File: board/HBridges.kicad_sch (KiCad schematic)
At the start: 36 parts, among them Q1 NMOS, Q2 NMOS, Q3 NMOS, Q4 NMOS, Q5 NMOS, Q6 NMOS

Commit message: Added CAN and Encoder connectors.
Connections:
- net VCC renamed VM
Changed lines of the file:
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@@
 			)
 		)
-		(property "Value" "VCC"
-			(at 41.91 22.86 0)
-			(effects
-				(font
-					(size 1.27 1.27)
-				)
+		(property "Value" "VM"
+			(at 44.45 26.6699 0)
+			(effects
+				(font
+					(size 1.27 1.27)
+				)
+				(justify left)
 			)
 		)
@@
 			)
 		)
-		(property "Value" "VCC"
-			(at 88.9 22.86 0)
-			(effects
-				(font
-					(size 1.27 1.27)
-				)
+		(property "Value" "VM"
+			(at 91.44 26.6699 0)
+			(effects
+				(font
+					(size 1.27 1.27)
+				)
+				(justify left)
 			)
 		)
@@
 			)
 		)
-		(property "Value" "VCC"
-			(at 135.89 22.86 0)
-			(effects
-				(font
-					(size 1.27 1.27)
-				)
-			)
-		)
+		(property "Value" "VM"
+			(at 138.43 26.6699 0)
+			(effects
+				(font
+					(size 1.27 1.27)
+				)
+				(justify left)
+			)
+		)

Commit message: Added some resistor and capacitor values.
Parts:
- C1, C10, C8: value C -> 30 nF
- R1, R11, R12, R2, R8, R9: value R -> 18 Ω
- R10, R13, R3: value R -> 1 mΩ / 1%
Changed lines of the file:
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@@
 			)
 		)
-		(property "Value" "R"
+		(property "Value" "18 Ω"
 			(at 121.92 39.37 90)
 			(effects
@@
 			)
 		)
-		(property "Value" "R"
+		(property "Value" "18 Ω"
 			(at 122.174 59.69 90)
 			(effects
@@
 			)
 		)
-		(property "Value" "R"
+		(property "Value" "18 Ω"
 			(at 28.194 59.69 90)
 			(effects
@@
 			)
 		)
-		(property "Value" "R"
+		(property "Value" "18 Ω"
 			(at 27.94 39.37 90)
 			(effects
@@
 			)
 		)
-		(property "Value" "R"
+		(property "Value" "18 Ω"
 			(at 75.184 59.69 90)
 			(effects
@@
 			)
 		)
-		(property "Value" "C"
+		(property "Value" "30 nF"
 			(at 129.794 50.8 90)
 			(effects
@@
 			)
 		)
-		(property "Value" "R"
-			(at 135.89 73.914 90)
+		(property "Value" "1 mΩ / 1%"
+			(at 133.604 73.66 90)
 			(effects
 				(font
@@
 			)
 		)
-		(property "Value" "R"
-			(at 41.91 73.914 90)
+		(property "Value" "1 mΩ / 1%"
+			(at 39.37 73.66 90)
 			(effects
 				(font
@@
 			)
 		)
-		(property "Value" "C"
+		(property "Value" "30 nF"
 			(at 82.804 50.8 90)
 			(effects
@@
 			)
 		)
-		(property "Value" "C"
+		(property "Value" "30 nF"
 			(at 35.814 50.8 90)
 			(effects
@@
 			)
 		)
-		(property "Value" "R"
-			(at 88.9 73.914 90)
+		(property "Value" "1 mΩ / 1%"
+			(at 86.868 73.914 90)
 			(effects
 				(font
@@
 			)
 		)
-		(property "Value" "R"
+		(property "Value" "18 Ω"
 			(at 74.93 39.37 90)
 			(effects

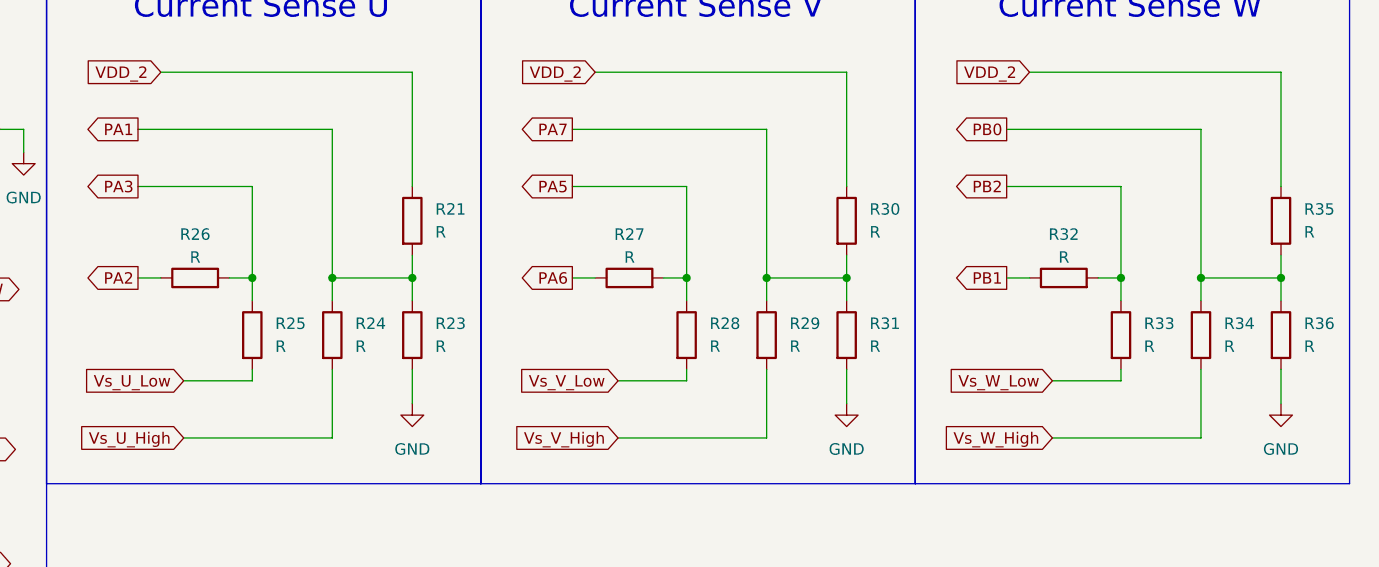
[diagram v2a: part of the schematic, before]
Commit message: Added resistor values to current sense circuit.
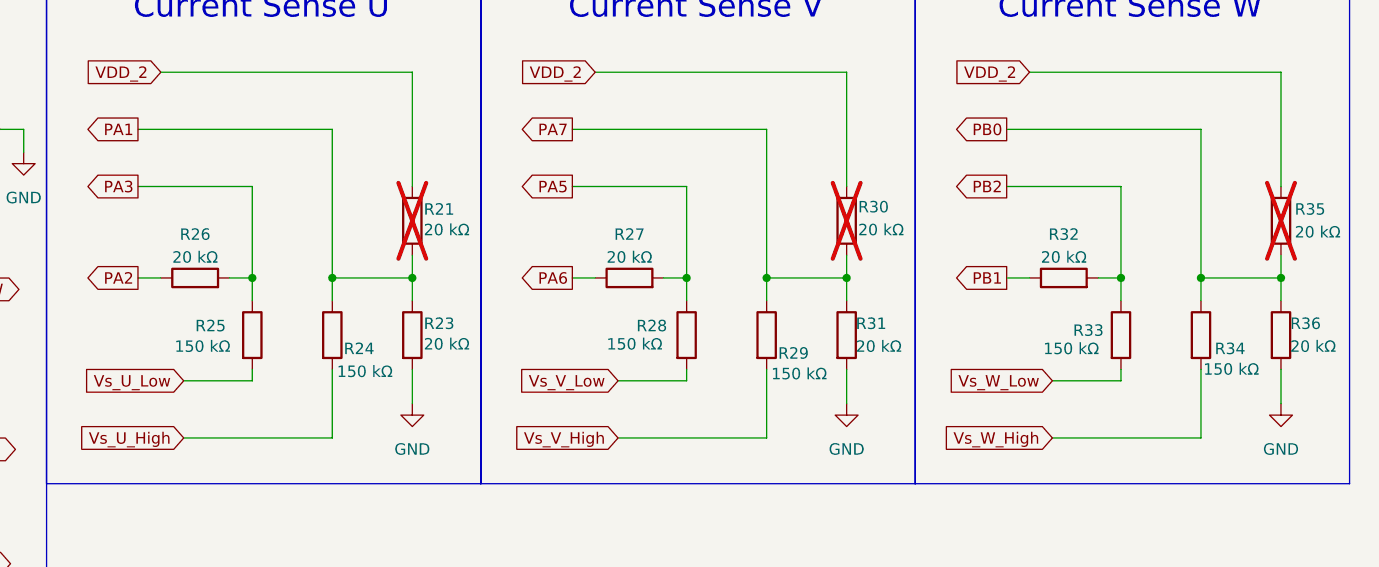
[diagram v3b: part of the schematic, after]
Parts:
- R21, R30, R35: value R -> 20 kΩ; now not fitted
- R23, R26, R27, R31, R32, R36: value R -> 20 kΩ
- R24, R25, R28, R29, R33, R34: value R -> 150 kΩ
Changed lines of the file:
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@@
 		(in_bom yes)
 		(on_board yes)
-		(dnp no)
-		(fields_autoplaced yes)
+		(dnp yes)
 		(property "Reference" "R30"
-			(at 245.11 40.6399 0)
-			(effects
-				(font
-					(size 1.27 1.27)
-				)
-				(justify left)
-			)
-		)
-		(property "Value" "R"
-			(at 245.11 43.1799 0)
+			(at 243.84 40.386 0)
+			(effects
+				(font
+					(size 1.27 1.27)
+				)
+				(justify left)
+			)
+		)
+		(property "Value" "20 kΩ"
+			(at 243.84 42.926 0)
 			(effects
 				(font
@@
 		(on_board yes)
 		(dnp no)
-		(fields_autoplaced yes)
 		(property "Reference" "R25"
-			(at 179.07 53.3399 0)
-			(effects
-				(font
-					(size 1.27 1.27)
-				)
-				(justify left)
-			)
-		)
-		(property "Value" "R"
-			(at 179.07 55.8799 0)
+			(at 170.18 53.594 0)
+			(effects
+				(font
+					(size 1.27 1.27)
+				)
+				(justify left)
+			)
+		)
+		(property "Value" "150 kΩ"
+			(at 167.894 55.88 0)
 			(effects
 				(font
@@
 			)
 		)
-		(property "Value" "R"
+		(property "Value" "20 kΩ"
 			(at 218.44 45.974 90)
 			(effects
@@
 		(in_bom yes)
 		(on_board yes)
-		(dnp no)
-		(fields_autoplaced yes)
+		(dnp yes)
 		(property "Reference" "R35"
-			(at 293.37 40.6399 0)
-			(effects
-				(font
-					(size 1.27 1.27)
-				)
-				(justify left)
-			)
-		)
-		(property "Value" "R"
-			(at 293.37 43.1799 0)
+			(at 292.354 40.64 0)
+			(effects
+				(font
+					(size 1.27 1.27)
+				)
+				(justify left)
+			)
+		)
+		(property "Value" "20 kΩ"
+			(at 292.354 43.18 0)
 			(effects
 				(font
@@
 			)
 		)
-		(property "Value" "R"
+		(property "Value" "20 kΩ"
 			(at 266.7 45.974 90)
 			(effects
@@
 		(in_bom yes)
 		(on_board yes)
-		(dnp no)
-		(fields_autoplaced yes)
+		(dnp yes)
 		(property "Reference" "R21"
-			(at 196.85 40.6399 0)
-			(effects
-				(font
-					(size 1.27 1.27)
-				)
-				(justify left)
-			)
-		)
-		(property "Value" "R"
-			(at 196.85 43.1799 0)
+			(at 195.58 40.64 0)
+			(effects
+				(font
+					(size 1.27 1.27)
+				)
+				(justify left)
+			)
+		)
+		(property "Value" "20 kΩ"
+			(at 195.58 42.926 0)
 			(effects
 				(font
@@
 		(on_board yes)
 		(dnp no)
-		(fields_autoplaced yes)
 		(property "Reference" "R33"
-			(at 275.59 53.3399 0)
-			(effects
-				(font
-					(size 1.27 1.27)
-				)
-				(justify left)
-			)
-		)
-		(property "Value" "R"
-			(at 275.59 55.8799 0)
+			(at 267.716 54.102 0)
+			(effects
+				(font
+					(size 1.27 1.27)
+				)
+				(justify left)
+			)
+		)
+		(property "Value" "150 kΩ"
+			(at 264.414 56.134 0)
 			(effects
 				(font
@@
 		(on_board yes)
 		(dnp no)
-		(fields_autoplaced yes)
 		(property "Reference" "R24"
-			(at 187.96 53.3399 0)
-			(effects
-				(font
-					(size 1.27 1.27)
-				)
-				(justify left)
-			)
-		)
-		(property "Value" "R"
-			(at 187.96 55.8799 0)
+			(at 186.69 56.134 0)
+			(effects
+				(font
+					(size 1.27 1.27)
+				)
+				(justify left)
+			)
+		)
+		(property "Value" "150 kΩ"
+			(at 185.928 58.674 0)
 			(effects
 				(font
@@
 		(on_board yes)
 		(dnp no)
-		(fields_autoplaced yes)
 		(property "Reference" "R31"
-			(at 245.11 53.3399 0)
-			(effects
-				(font
-					(size 1.27 1.27)
-				)
-				(justify left)
-			)
-		)
-		(property "Value" "R"
-			(at 245.11 55.8799 0)
+			(at 243.586 53.34 0)
+			(effects
+				(font
+					(size 1.27 1.27)
+				)
+				(justify left)
+			)
+		)
+		(property "Value" "20 kΩ"
+			(at 243.586 55.88 0)
 			(effects
 				(font
@@
 		(on_board yes)
 		(dnp no)
-		(fields_autoplaced yes)
 		(property "Reference" "R34"
-			(at 284.48 53.3399 0)
-			(effects
-				(font
-					(size 1.27 1.27)
-				)
-				(justify left)
-			)
-		)
-		(property "Value" "R"
-			(at 284.48 55.8799 0)
+			(at 283.464 56.134 0)
+			(effects
+				(font
+					(size 1.27 1.27)
+				)
+				(justify left)
+			)
+		)
+		(property "Value" "150 kΩ"
+			(at 282.194 58.42 0)
 			(effects
 				(font
@@
 		(on_board yes)
 		(dnp no)
-		(fields_autoplaced yes)
 		(property "Reference" "R28"
-			(at 227.33 53.3399 0)
-			(effects
-				(font
-					(size 1.27 1.27)
-				)
-				(justify left)
-			)
-		)
-		(property "Value" "R"
-			(at 227.33 55.8799 0)
+			(at 219.202 53.594 0)
+			(effects
+				(font
+					(size 1.27 1.27)
+				)
+				(justify left)
+			)
+		)
+		(property "Value" "150 kΩ"
+			(at 215.9 55.626 0)
 			(effects
 				(font
@@
 		(on_board yes)
 		(dnp no)
-		(fields_autoplaced yes)
 		(property "Reference" "R23"
-			(at 196.85 53.3399 0)
-			(effects
-				(font
-					(size 1.27 1.27)
-				)
-				(justify left)
-			)
-		)
-		(property "Value" "R"
-			(at 196.85 55.8799 0)
+			(at 195.58 53.34 0)
+			(effects
+				(font
+					(size 1.27 1.27)
+				)
+				(justify left)
+			)
+		)
+		(property "Value" "20 kΩ"
+			(at 195.58 55.626 0)
 			(effects
 				(font
@@
 			)
 		)
-		(property "Value" "R"
+		(property "Value" "20 kΩ"
 			(at 170.18 45.974 90)
 			(effects
@@
 		(on_board yes)
 		(dnp no)
-		(fields_autoplaced yes)
 		(property "Reference" "R29"
-			(at 236.22 53.3399 0)
-			(effects
-				(font
-					(size 1.27 1.27)
-				)
-				(justify left)
-			)
-		)
-		(property "Value" "R"
-			(at 236.22 55.8799 0)
+			(at 234.95 56.642 0)
+			(effects
+				(font
+					(size 1.27 1.27)
+				)
+				(justify left)
+			)
+		)
+		(property "Value" "150 kΩ"
+			(at 234.188 58.928 0)
 			(effects
 				(font
@@
 		(on_board yes)
 		(dnp no)
-		(fields_autoplaced yes)
 		(property "Reference" "R36"
-			(at 293.37 53.3399 0)
-			(effects
-				(font
-					(size 1.27 1.27)
-				)
-				(justify left)
-			)
-		)
-		(property "Value" "R"
-			(at 293.37 55.8799 0)
-			(effects
-				(font
+			(at 291.846 53.34 0)
+			(effects
+				(font
+					(size 1.27 1.27)
+				)
+				(justify left)
+			)
+		)
+		(property "Value" "20 kΩ"
+			(at 291.846 55.88 0)
+			(effects
+				(font

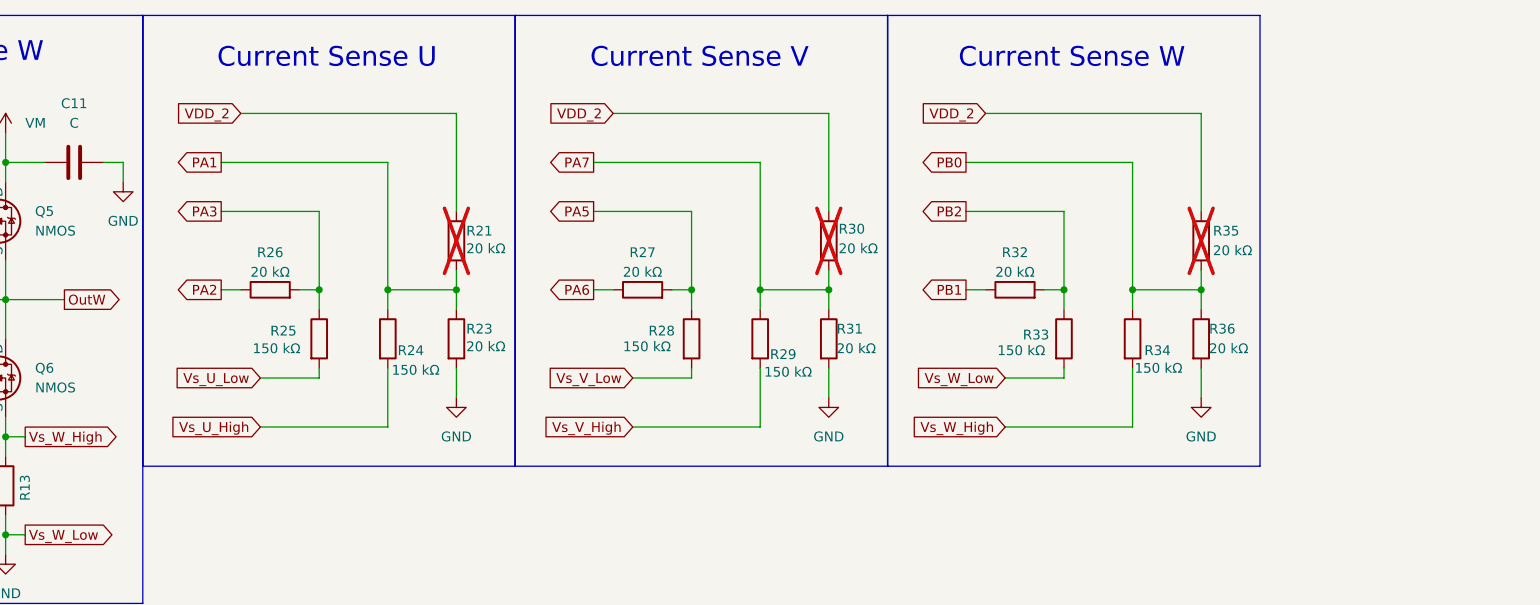
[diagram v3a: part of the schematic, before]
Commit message: Finished adding component values to circuits, except for 4 filtering capacitors
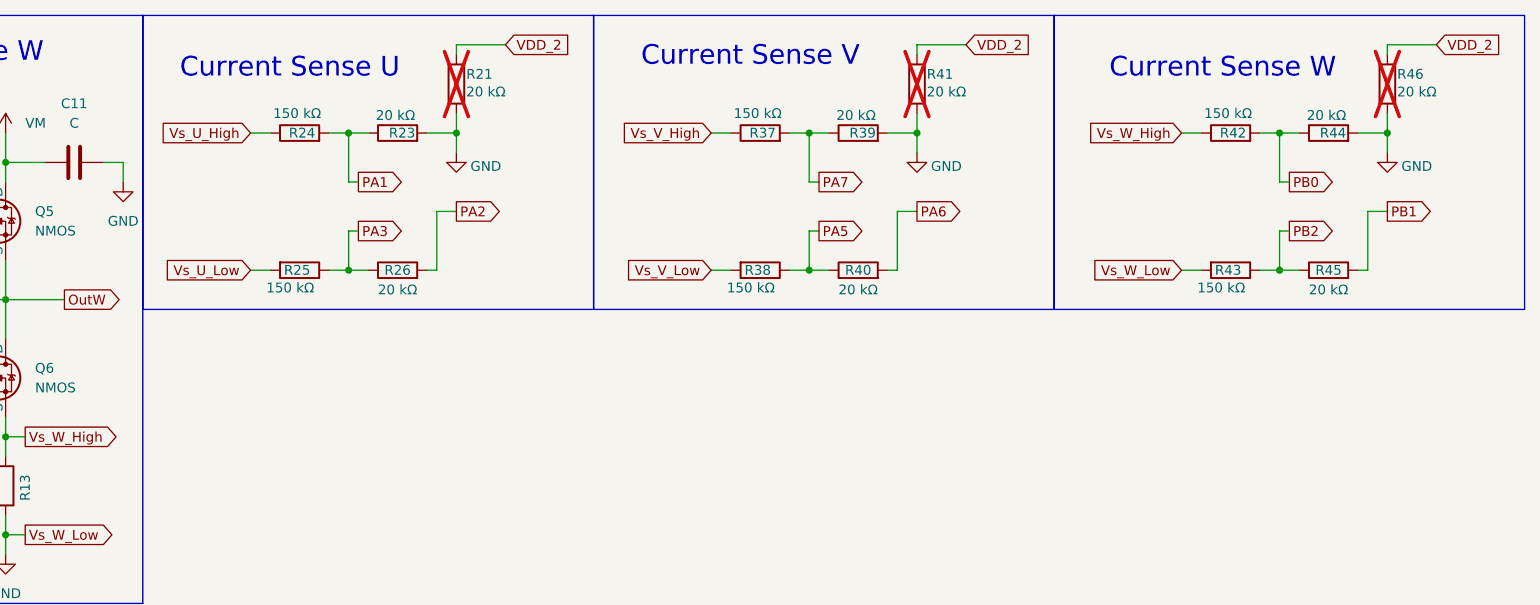
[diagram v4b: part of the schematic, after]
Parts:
- removed R27, R30, R31, R32, R35, R36: 20 kΩ, symbol Device:R
- removed R28, R29, R33, R34: 150 kΩ, symbol Device:R
- added R37, R38, R42, R43: 150 kΩ, symbol Device:R
- added R39, R40, R41, R44, R45, R46: 20 kΩ, symbol Device:R
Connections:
- net GND: now also R21.2, R38.2, R39.2, R41.2, R43.2, R44.2, R46.2
- net PA1: now also R24.2; no longer R21.2, R24.1
- net PA2: now also R26.2; no longer R26.1
- net PA3: now also R26.1; no longer R26.2
- net PA5: now also R38.1, R40.1
- net PA6: now also R40.2
- net PA7: now also R37.2, R39.1
- net PB0: now also R42.2, R44.1
- net PB1: now also R45.2
- net PB2: now also R43.1, R45.1
- net VDD_2: now also R41.1, R46.1
- net Vs_U_High: now also R24.1; no longer R24.2
- net Vs_V_High: now also R37.1
- net Vs_W_High: now also R42.1
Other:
- moved on the sheet: R21, R23, R24, R25, R26

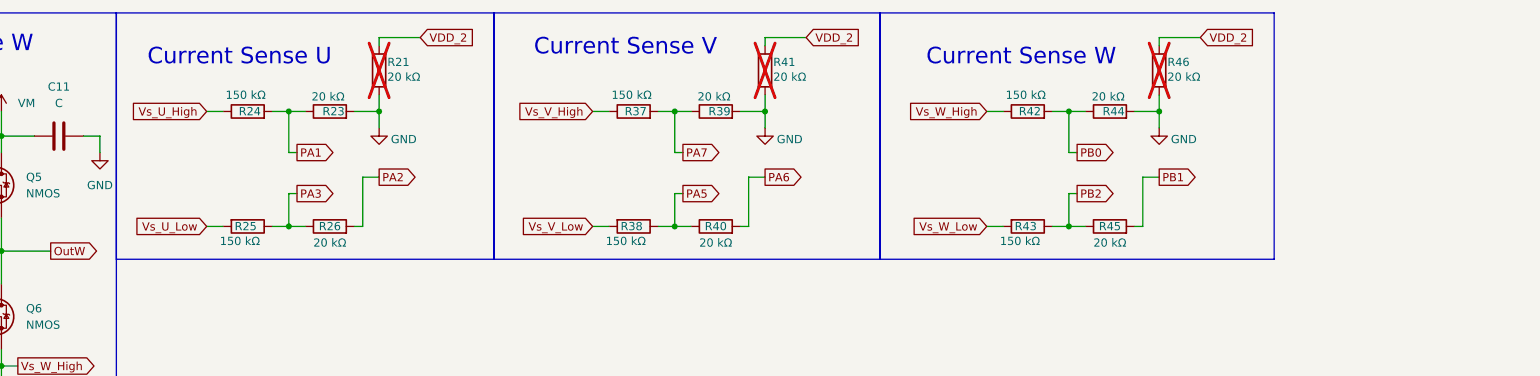
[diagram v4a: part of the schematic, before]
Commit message: Implemented some fixes discussed during the board review.
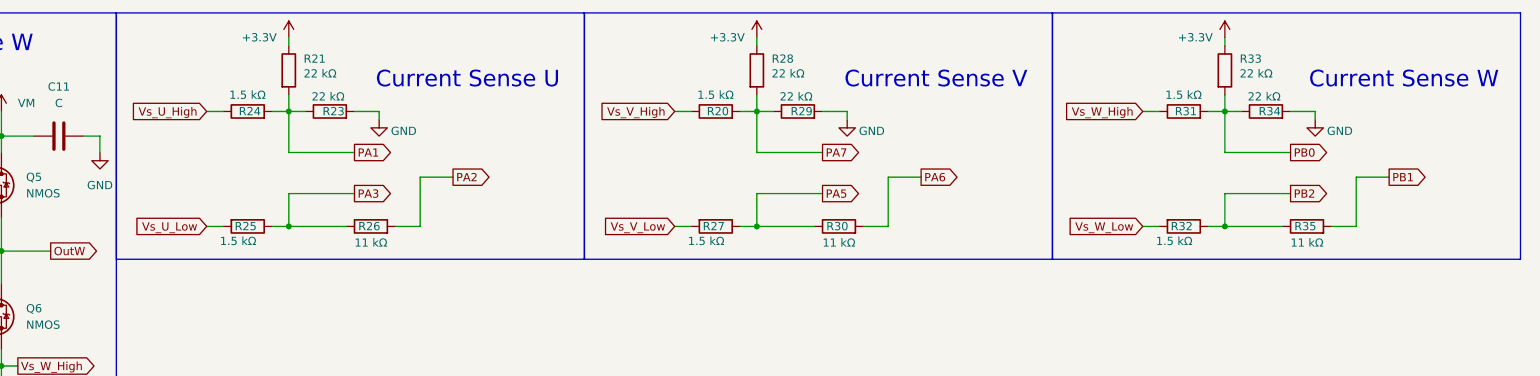
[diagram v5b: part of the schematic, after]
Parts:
- removed R37, R38, R42, R43: 150 kΩ, symbol Device:R
- removed R39, R40, R41, R44, R45, R46: 20 kΩ, symbol Device:R
- added R20, R27, R31, R32: 1.5 kΩ, symbol Device:R
- added R28, R29, R33, R34: 22 kΩ, symbol Device:R
- added R30, R35: 11 kΩ, symbol Device:R
- R21: value 20 kΩ -> 22 kΩ; now fitted
- R23: value 20 kΩ -> 22 kΩ
- R24, R25: value 150 kΩ -> 1.5 kΩ
- R26: value 20 kΩ -> 11 kΩ
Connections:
- net GND: now also R27.2, R29.2, R32.2, R34.2; no longer R21.2
- net PA1: now also R21.2
- net PA5: now also R27.1, R30.1
- net PA6: now also R30.2
- net PA7: now also R20.2, R28.2, R29.1
- net PB0: now also R31.2, R33.2, R34.1
- net PB1: now also R35.2
- net PB2: now also R32.1, R35.1
- net Vs_V_High: now also R20.1
- net Vs_W_High: now also R31.1
- net VDD_2 renamed +3.3V
- net +3.3V: now also R28.1, R33.1
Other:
- moved on the sheet: R26
